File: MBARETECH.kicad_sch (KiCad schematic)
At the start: 48 parts, among them J10 Conn_01x03, J11 Conn_01x03, J17 Conn_01x03, J18 Conn_01x03, J19 TERMINAL DRIVER, J3 XT60-M, J7 Conn_01x03, J8 Conn_01x03, J9 Conn_01x03, SW1 SW_SPDT, SW2 SW_DIP_x04, SW3 SW_SPDT, SW5 SW_SPST, U2 ESP32-S3-DevKitC

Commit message: Version final
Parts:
- removed D1: D, symbol Device:D
- removed F1: Fuse, symbol Device:Fuse
- removed J19: TERMINAL DRIVER, symbol Connector:Screw_Terminal_01x02
- removed J3: XT60-M, XT60-M:AMASS_XT60-M, symbol XT60-M:XT60-M
- removed R20: R, symbol Device:R
- removed SW5: SW_SPST, symbol Switch:SW_SPST
- removed U2: ESP32-S3-DevKitC, PCM_Espressif:ESP32-S3-DevKitC, symbol Espressif:ESP32-S3-DevKitC
- added DRIVER1: DRIVER, TerminalBlock_Phoenix:TerminalBlock_Phoenix_MKDS-1,5-2-5.08_1x02_P5.08mm_Horizontal, symbol Connector:Screw_Terminal_01x02
- added IR6_NPN1: IR6, Connector_JST:JST_XH_B3B-XH-A_1x03_P2.50mm_Vertical, symbol Connector_Generic:Conn_01x03
- added IR7: IR7_NPN, Connector_JST:JST_XH_B3B-XH-A_1x03_P2.50mm_Vertical, symbol Connector_Generic:Conn_01x03
- added PWR1: PWR, TerminalBlock_Phoenix:TerminalBlock_Phoenix_MKDS-1,5-2-5.08_1x02_P5.08mm_Horizontal, symbol Connector:Screw_Terminal_01x02
- added R6, R7: 1Ok, Resistor_SMD:R_0603_1608Metric_Pad0.98x0.95mm_HandSolder, symbol Device:R
- added U1: ESP32-S3-DEVKITC-1-N8R2, ESP32-S3-DEVKITC-1-N8R2:XCVR_ESP32-S3-DEVKITC-1-N8R2, symbol ESP32-S3-DEVKITC-1-N8R2:ESP32-S3-DEVKITC-1-N8R2
- BUCK1: renamed from U3; value ~ -> BUCK_24V; footprint (none) -> Mbaretech_buckConverter:Buck-Converter
- BUCK2: renamed from U1; value ~ -> BUCK_3V3; footprint (none) -> Mbaretech_buckConverter:Buck-Converter
- Boost1: value ~ -> BOOST; footprint (none) -> Connector_PinHeader_2.54mm:PinHeader_1x03_P2.54mm_Vertical
- DIP1: renamed from SW2; value SW_DIP_x04 -> DIP; footprint (none) -> Button_Switch_THT:SW_DIP_SPSTx04_Slide_9.78x12.34mm_W7.62mm_P2.54mm
- EA1: renamed from J2; value ~ -> EA; footprint Connector_JST:JST_PH_B9B-PH-K_1x09_P2.00mm_Vertical -> Connector_JST:JST_XH_B3B-XH-A_1x03_P2.50mm_Vertical
- EB1: renamed from J4; value ~ -> EB; footprint Connector_JST:JST_PH_B9B-PH-K_1x09_P2.00mm_Vertical -> Connector_JST:JST_XH_B3B-XH-A_1x03_P2.50mm_Vertical
- HALL1: renamed from J5; value ~ -> HALL; footprint Connector_JST:JST_PH_B9B-PH-K_1x09_P2.00mm_Vertical -> Connector_JST:JST_XH_B3B-XH-A_1x03_P2.50mm_Vertical
- IMU1: renamed from U4; value ~ -> IMU; footprint (none) -> Connector_PinHeader_2.54mm:PinHeader_1x10_P2.54mm_Vertical
- IR1: renamed from J17; value Conn_01x03 -> IR1; footprint Connector_AMASS:AMASS_XT60-F_1x02_P7.20mm_Vertical -> Connector_JST:JST_XH_B3B-XH-A_1x03_P2.50mm_Vertical
- IR2: renamed from J7; value Conn_01x03 -> IR2; footprint Connector_AMASS:AMASS_XT60-F_1x02_P7.20mm_Vertical -> Connector_JST:JST_XH_B3B-XH-A_1x03_P2.50mm_Vertical
- IR3: renamed from J8; value Conn_01x03 -> IR3; footprint Connector_AMASS:AMASS_XT60-F_1x02_P7.20mm_Vertical -> Connector_JST:JST_XH_B3B-XH-A_1x03_P2.50mm_Vertical
- IR4: renamed from J9; value Conn_01x03 -> IR4; footprint Connector_AMASS:AMASS_XT60-F_1x02_P7.20mm_Vertical -> Connector_JST:JST_XH_B3B-XH-A_1x03_P2.50mm_Vertical
- IR5: renamed from J10; value Conn_01x03 -> IR5; footprint Connector_AMASS:AMASS_XT60-F_1x02_P7.20mm_Vertical -> Connector_JST:JST_XH_B3B-XH-A_1x03_P2.50mm_Vertical
- IR8: renamed from J18; value Conn_01x03 -> IR8_PNP; footprint Connector_AMASS:AMASS_XT60-F_1x02_P7.20mm_Vertical -> Connector_JST:JST_XH_B3B-XH-A_1x03_P2.50mm_Vertical
- IR9: renamed from J11; value Conn_01x03 -> IR9_PNP; footprint Connector_AMASS:AMASS_XT60-F_1x02_P7.20mm_Vertical -> Connector_JST:JST_XH_B3B-XH-A_1x03_P2.50mm_Vertical
- KS1: renamed from J6; value ~ -> KS; footprint Connector_JST:JST_PH_B9B-PH-K_1x09_P2.00mm_Vertical -> Connector_JST:JST_XH_B3B-XH-A_1x03_P2.50mm_Vertical
- LS1: renamed from J14; value ~ -> LS1; footprint Connector_JST:JST_PH_B9B-PH-K_1x09_P2.00mm_Vertical -> Connector_JST:JST_XH_B3B-XH-A_1x03_P2.50mm_Vertical
- LS2: renamed from J15; value ~ -> LS2; footprint Connector_JST:JST_PH_B9B-PH-K_1x09_P2.00mm_Vertical -> Connector_JST:JST_XH_B3B-XH-A_1x03_P2.50mm_Vertical
- LS3: renamed from J1; value ~ -> LS3; footprint Connector_JST:JST_PH_B9B-PH-K_1x09_P2.00mm_Vertical -> Connector_JST:JST_XH_B3B-XH-A_1x03_P2.50mm_Vertical
- LS4: renamed from J16; value ~ -> LS4; footprint Connector_JST:JST_PH_B9B-PH-K_1x09_P2.00mm_Vertical -> Connector_JST:JST_XH_B3B-XH-A_1x03_P2.50mm_Vertical
- MA1: renamed from J12; value ~ -> MA; footprint Connector_JST:JST_PH_B9B-PH-K_1x09_P2.00mm_Vertical -> Connector_JST:JST_XH_B3B-XH-A_1x03_P2.50mm_Vertical
- MB1: renamed from J13; value ~ -> MB; footprint Connector_JST:JST_PH_B9B-PH-K_1x09_P2.00mm_Vertical -> Connector_JST:JST_XH_B3B-XH-A_1x03_P2.50mm_Vertical
- R1, R10, R11, R2: footprint (none) -> Resistor_SMD:R_0603_1608Metric_Pad0.98x0.95mm_HandSolder
- R12: renamed from R3; footprint (none) -> Resistor_SMD:R_0603_1608Metric_Pad0.98x0.95mm_HandSolder
- R13: renamed from R7; footprint (none) -> Resistor_SMD:R_0603_1608Metric_Pad0.98x0.95mm_HandSolder
- R14: renamed from R4; value `5k -> 5k; footprint (none) -> Resistor_SMD:R_0603_1608Metric_Pad0.98x0.95mm_HandSolder
- R15: renamed from R5; footprint (none) -> Resistor_SMD:R_0603_1608Metric_Pad0.98x0.95mm_HandSolder
- R16: renamed from R14; footprint (none) -> Resistor_SMD:R_0603_1608Metric_Pad0.98x0.95mm_HandSolder
- R17: renamed from R15; footprint (none) -> Resistor_SMD:R_0603_1608Metric_Pad0.98x0.95mm_HandSolder
- R18: renamed from R16; footprint (none) -> Resistor_SMD:R_0603_1608Metric_Pad0.98x0.95mm_HandSolder
- R19: renamed from R17; footprint (none) -> Resistor_SMD:R_0603_1608Metric_Pad0.98x0.95mm_HandSolder
- R3: renamed from R6; footprint (none) -> Resistor_SMD:R_0603_1608Metric_Pad0.98x0.95mm_HandSolder
- R4: renamed from R8; footprint (none) -> Resistor_SMD:R_0603_1608Metric_Pad0.98x0.95mm_HandSolder
- R5: renamed from R9; footprint (none) -> Resistor_SMD:R_0603_1608Metric_Pad0.98x0.95mm_HandSolder
- R8: renamed from R18; footprint (none) -> Resistor_SMD:R_0603_1608Metric_Pad0.98x0.95mm_HandSolder
- R9: renamed from R19; footprint (none) -> Resistor_SMD:R_0603_1608Metric_Pad0.98x0.95mm_HandSolder
- SW1: value SW_SPDT -> SW1; footprint (none) -> SPDT_SlideSwitch:tht
- SW2: renamed from SW3; value SW_SPDT -> SW2; footprint (none) -> SPDT_SlideSwitch:tht
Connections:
- net 24V is gone; now on net +24V: BUCK1.4 (VOUT)
- net GNDS is gone; now on net GND: IR2.3 (Pin_3), IR4.3 (Pin_3)
- net +24V: now also IR8.1 (Pin_1), IR9.1 (Pin_1), IR6_NPN1.1 (Pin_1), IR7.1 (Pin_1); no longer IR8.3 (Pin_3), IR9.3 (Pin_3)
- net +3V3: now also R2.1, R6.1, R7.1, U1.J1_1 (3V3), U1.J1_2 (3V3); no longer R13.1
- net +5V: now also DRIVER1.1 (Pin_1)
- net +BATT: now also PWR1.1 (Pin_1)
- net -BATT: now also PWR1.2 (Pin_2)
- net A0: now also U1.J3_15 (GPIO45)
- net A1: now also U1.J3_16 (GPIO48)
- net B0: now also U1.J3_12 (GPIO36)
- net B1: now also U1.J3_13 (GPIO35)
- net ENCODER_A_3V3: now also R13.1, U1.J1_20 (GPIO14); no longer R2.1
- net ENCODER_B_3V3: now also U1.J1_18 (GPIO12)
- net GND: now also IR8.3 (Pin_3), IR9.3 (Pin_3), R13.2, DRIVER1.2 (Pin_2), IR6_NPN1.3 (Pin_3), IR7.3 (Pin_3), U1.J1_22 (GND), U1.J3_1 (GND), U1.J3_21 (GND), U1.J3_22 (GND); no longer IR8.1 (Pin_1), IR9.1 (Pin_1), R2.2
- net HALL_3V3: now also U1.J3_2 (U0TXD/GPIO43)
- net IR1_3V3: now also R1.2, U1.J3_8 (MTDO/GPIO40); no longer R13.2
- net IR2_3V3: now also R2.2, U1.J3_9 (MTCK/GPIO39); no longer R1.2
- net IR3_3V3: now also U1.J3_10 (GPIO38)
- net IR4_3V3: now also U1.J1_11 (GPIO18)
- net IR5_3V3: now also U1.J1_10 (GPIO17)
- net IR6_3V3: now also IR6_NPN1.2 (Pin_2), R6.2, U1.J1_4 (GPIO4); no longer R8.1, R9.1
- net IR7_3V3: now also IR7.2 (Pin_2), R7.2, U1.J1_5 (GPIO5); no longer R10.1, R11.1
- net KILLSWITCH: now also U1.J3_7 (MTDI/GPIO41)
- net LS1_3V3: now also U1.J1_13 (GPIO3)
- net LS2_3V3: now also U1.J1_12 (GPIO8)
- net LS3_3V3: now also U1.J3_19 (USB_D+/GPIO20)
- net LS4_3V3: now also U1.J3_20 (USB_D-/GPIO19)
- net PWMA: now also U1.J3_14 (GPIO0)
- net PWMB: now also U1.J3_11 (GPIO37)
- net S1: now also U1.J3_6 (MTMS/GPIO42)
- net S2: now also U1.J3_5 (GPIO2)
- net S3: now also U1.J3_4 (GPIO1)
- net S4: now also U1.J3_3 (U0RXD/GPIO44)
- net SCL: now also U1.J1_9 (GPIO16)
- net SDA: now also U1.J1_8 (GPIO15)
- net IMU_INT: no longer names the net of IMU1.8 (INT)
- net IR6_24V renamed IR8_24V
- net IR7_24V renamed IR9_24V
- new net IR8_3V3_PNP: R8.1, R9.1, U1.J1_6 (GPIO6)
- new net IR9_3V3_PNP: R10.1, R11.1, U1.J1_7 (GPIO7)
- no-connect marks 8 -> 17
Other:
- moved on the sheet: BUCK1, BUCK2, Boost1, DIP1, EA1, EB1, HALL1, IMU1, IR2, IR3, IR4, IR5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

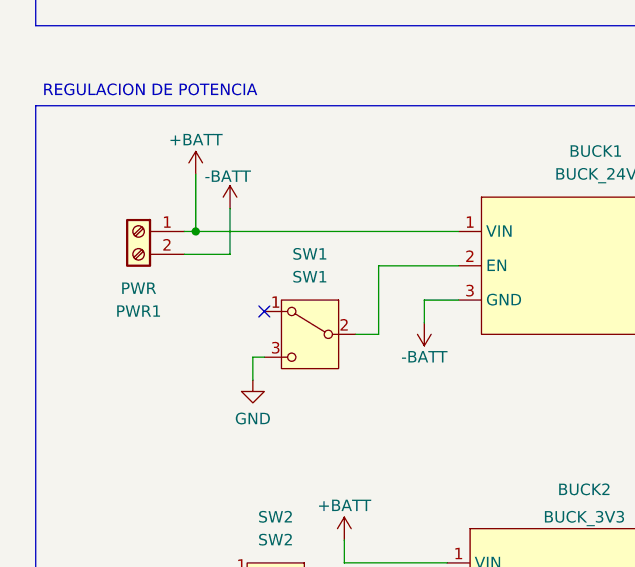
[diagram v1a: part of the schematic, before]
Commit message: Connect -BATT2GND
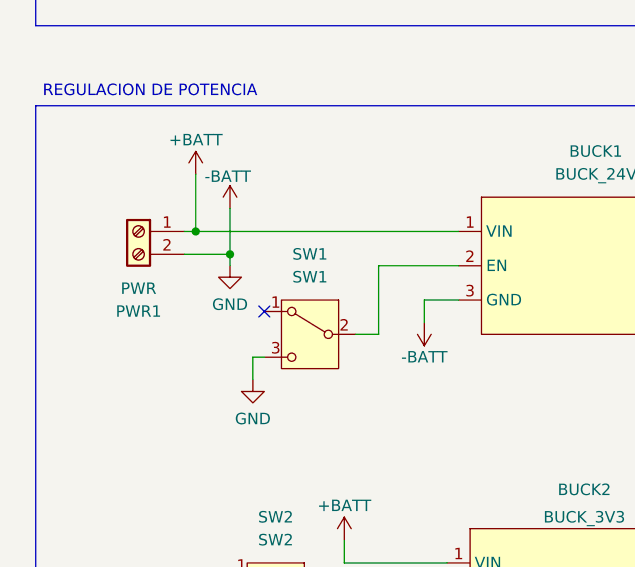
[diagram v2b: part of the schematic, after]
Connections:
- net GND is gone; now on net -BATT: BUCK1.5 (GND), BUCK2.5 (GND), Boost1.2 (GND), DRIVER1.2 (Pin_2), EA1.3 (Pin_3), EB1.3 (Pin_3), HALL1.3 (Pin_3), IMU1.2 (GND), IR1.3 (Pin_3), IR2.3 (Pin_3), IR3.3 (Pin_3), IR4.3 (Pin_3), IR5.3 (Pin_3), IR6_NPN1.3 (Pin_3), IR7.3 (Pin_3), IR8.3 (Pin_3), IR9.3 (Pin_3), KS1.3 (Pin_3), LS1.3 (Pin_3), LS2.3 (Pin_3), LS3.3 (Pin_3), LS4.3 (Pin_3), R11.2, R13.2, R15.2, R16.2, R17.2, R18.2, R19.2, R9.2, SW1.3 (C), SW2.3 (C), U1.J1_22 (GND), U1.J3_1 (GND), U1.J3_21 (GND), U1.J3_22 (GND)
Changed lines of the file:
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@@
 		(color 0 0 0 0)
 	)
+	(junction
+		(at 59.69 143.51)
+		(diameter 0)
+		(color 0 0 0 0)
+	)
 	(no_connect
 		(at 109.22 39.37)
@@
 	(wire
 		(pts
+			(xy 59.69 144.78) (xy 59.69 143.51)
+		)
+		(stroke
+			(width 0)
+			(type default)
+		)
+	)
+	(wire
+		(pts
 			(xy 90.17 209.55) (xy 90.17 210.82)
 		)
@@
 					(unit 1)
 				)
+			)
+		)
+	)
+	(symbol
+		(lib_id "power:GND")
+		(at 59.69 144.78 0)
+		(unit 1)
+		(exclude_from_sim no)
+		(in_bom yes)
+		(on_board yes)
+		(dnp no)
+		(property "Reference" "#PWR01"
+			(at 59.69 151.13 0)
+			(effects
+				(font
+					(size 1.27 1.27)
+				)
+				(hide yes)
+			)
+		)
+		(property "Value" "GND"
+			(at 59.69 149.098 0)
+			(effects
+				(font
+					(size 1.27 1.27)
+				)
+			)
+		)
+		(property "Footprint" ""
+			(at 59.69 144.78 0)
+			(effects
+				(font
+					(size 1.27 1.27)
+				)
+				(hide yes)
+			)
+		)
+		(property "Datasheet" ""
+			(at 59.69 144.78 0)
+			(effects
+				(font
+					(size 1.27 1.27)
+				)
+				(hide yes)
+			)
+		)
+		(property "Description" "Power symbol creates a global label with name \"GND\" , ground"
+			(at 59.69 144.78 0)
+			(effects
+				(font
+					(size 1.27 1.27)
+				)
+				(hide yes)
+			)
+		)
+		(pin "1"
+		)
+		(instances
+			(project "MBARETECH"
+				(path "/22b8a1e8-4df5-4930-9e5c-6226e609bfdf"
+					(reference "#PWR01")
+					(unit 1)
+				)

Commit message: final
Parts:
- R1: value 1Ok -> R1
- R10: value R -> R10
- R11: value R -> R11
- R12: value `5k -> R12
- R13: value 1Ok -> R13
- R14: value 5k -> R14
- R15: value 10k -> R15
- R16: value 10k -> R16
- R17: value 10k -> R17
- R18: value 10k -> R18
- R19: value 10k -> R19
- R2: value 10k -> R2
- R3: value 1Ok -> R3
- R4: value 1Ok -> R4
- R5: value 1Ok -> R5
- R6: value 1Ok -> R6
- R7: value 1Ok -> R7
- R8: value R -> R8
- R9: value R -> R9
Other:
- moved on the sheet: SW1
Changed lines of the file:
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@@
 	)
 	(junction
+		(at 55.88 143.51)
+		(diameter 0)
+		(color 0 0 0 0)
+	)
+	(junction
 		(at 55.88 140.97)
 		(diameter 0)
@@
 		(color 0 0 0 0)
 	)
-	(junction
-		(at 59.69 143.51)
-		(diameter 0)
-		(color 0 0 0 0)
-	)
 	(no_connect
 		(at 109.22 39.37)
@@
 	)
 	(no_connect
-		(at 63.5 149.86)
+		(at 64.77 149.86)
 	)
 	(no_connect
@@
 	(wire
 		(pts
-			(xy 59.69 138.43) (xy 59.69 143.51)
+			(xy 55.88 144.78) (xy 55.88 143.51)
 		)
 		(stroke
@@
 	(wire
 		(pts
-			(xy 62.23 154.94) (xy 63.5 154.94)
+			(xy 62.23 154.94) (xy 64.77 154.94)
 		)
 		(stroke
@@
 	(wire
 		(pts
-			(xy 76.2 152.4) (xy 73.66 152.4)
+			(xy 76.2 152.4) (xy 74.93 152.4)
 		)
 		(stroke
@@
 	(wire
 		(pts
+			(xy 60.96 144.78) (xy 60.96 143.51)
+		)
+		(stroke
+			(width 0)
+			(type default)
+		)
+	)
+	(wire
+		(pts
 			(xy 115.57 140.97) (xy 118.11 140.97)
 		)
@@
 	(wire
 		(pts
-			(xy 54.61 143.51) (xy 59.69 143.51)
+			(xy 54.61 143.51) (xy 55.88 143.51)
 		)
 		(stroke
@@
 	(wire
 		(pts
+			(xy 55.88 143.51) (xy 60.96 143.51)
+		)
+		(stroke
+			(width 0)
+			(type default)
+		)
+	)
+	(wire
+		(pts
 			(xy 350.52 33.02) (xy 350.52 40.64)
 		)
@@
 	(wire
 		(pts
-			(xy 59.69 144.78) (xy 59.69 143.51)
-		)
-		(stroke
-			(width 0)
-			(type default)
-		)
-	)
-	(wire
-		(pts
 			(xy 90.17 209.55) (xy 90.17 210.82)
 		)
@@
 			)
 		)
-		(property "Value" "10k"
+		(property "Value" "R19"
 			(at 220.218 238.76 0)
 			(effects
@@
 			)
 		)
-		(property "Value" "10k"
+		(property "Value" "R16"
 			(at 200.66 238.76 0)
 			(effects
@@
 	(symbol
 		(lib_id "power:+BATT")
-		(at 59.69 138.43 0)
+		(at 55.88 144.78 180)
 		(unit 1)
 		(exclude_from_sim no)
@@
 		(dnp no)
 		(property "Reference" "#PWR042"
-			(at 59.69 142.24 0)
+			(at 55.88 140.97 0)
 			(effects
 				(font
@@
 		)
 		(property "Value" "-BATT"
-			(at 59.436 134.874 0)
+			(at 56.134 148.336 0)
 			(effects
 				(font
@@
 		)
 		(property "Footprint" ""
-			(at 59.69 138.43 0)
+			(at 55.88 144.78 0)
 			(effects
 				(font
@@
 		)
 		(property "Datasheet" ""
-			(at 59.69 138.43 0)
+			(at 55.88 144.78 0)
 			(effects
 				(font
@@
 		)
 		(property "Description" "Power symbol creates a global label with name \"+BATT\""
-			(at 59.69 138.43 0)
+			(at 55.88 144.78 0)
 			(effects
 				(font
@@
 			)
 		)
-		(property "Value" "R"
+		(property "Value" "R10"
 			(at 314.96 232.41 90)
 			(effects
@@
 			)
 		)
-		(property "Value" "1Ok"
+		(property "Value" "R5"
 			(at 313.69 115.5699 0)
 			(effects
@@
 			)
 		)
-		(property "Value" "1Ok"
+		(property "Value" "R4"
 			(at 365.76 77.4699 0)
 			(effects
@@
 			)
 		)
-		(property "Value" "R"
+		(property "Value" "R8"
 			(at 312.42 198.12 90)
 			(effects
@@
 			)
 		)
-		(property "Value" "1Ok"
+		(property "Value" "R3"
 			(at 313.69 76.1999 0)
 			(effects
@@
 			)
 		)
-		(property "Value" "R"
+		(property "Value" "R11"
 			(at 322.58 233.6799 0)
 			(effects
@@
 			)
 		)
-		(property "Value" "5k"
+		(property "Value" "R14"
 			(at 193.04 165.1 0)
 			(effects
@@
 			)
 		)
-		(property "Value" "1Ok"
+		(property "Value" "R7"
 			(at 317.5 151.1299 0)
 			(effects
@@
 			)
 		)
-		(property "Value" "1Ok"
+		(property "Value" "R1"
 			(at 313.69 39.3699 0)
 			(effects
@@
 			)
 		)
-		(property "Value" "10k"
+		(property "Value" "R15"
 			(at 200.66 172.72 0)
 			(effects
@@
 	)
 	(symbol
+		(lib_id "power:GND")
+		(at 60.96 144.78 0)
+		(unit 1)
+		(exclude_from_sim no)
+		(in_bom yes)
+		(on_board yes)
+		(dnp no)
+		(property "Reference" "#PWR03"
+			(at 60.96 151.13 0)
+			(effects
+				(font
+					(size 1.27 1.27)
+				)
+				(hide yes)
+			)
+		)
+		(property "Value" "GND"
+			(at 60.96 149.098 0)
+			(effects
+				(font
+					(size 1.27 1.27)
+				)
+			)
+		)
+		(property "Footprint" ""
+			(at 60.96 144.78 0)
+			(effects
+				(font
+					(size 1.27 1.27)
+				)
+				(hide yes)
+			)
+		)
+		(property "Datasheet" ""
+			(at 60.96 144.78 0)
+			(effects
+				(font
+					(size 1.27 1.27)
+				)
+				(hide yes)
+			)
+		)
+		(property "Description" "Power symbol creates a global label with name \"GND\" , ground"
+			(at 60.96 144.78 0)
+			(effects
+				(font
+					(size 1.27 1.27)
+				)
+				(hide yes)
+			)
+		)
+		(pin "1"
+		)
+		(instances
+			(project "MBARETECH"
+				(path "/22b8a1e8-4df5-4930-9e5c-6226e609bfdf"
+					(reference "#PWR03")
+					(unit 1)
+				)
+			)
+		)
+	)
+	(symbol
 		(lib_id "power:+3V3")
 		(at 213.36 35.56 0)
@@
 			)
 		)
-		(property "Value" "10k"
+		(property "Value" "R2"
 			(at 361.95 39.37 0)
 			(effects
@@
 	(symbol
 		(lib_id "power:GND")
-		(at 59.69 144.78 0)
-		(unit 1)
-		(exclude_from_sim no)
-		(in_bom yes)
-		(on_board yes)
-		(dnp no)
-		(property "Reference" "#PWR01"
-			(at 59.69 151.13 0)
-			(effects
-				(font
-					(size 1.27 1.27)
-				)
-				(hide yes)
-			)
-		)
-		(property "Value" "GND"
-			(at 59.69 149.098 0)
-			(effects
-				(font
-					(size 1.27 1.27)
-				)
-			)
-		)
-		(property "Footprint" ""
-			(at 59.69 144.78 0)
-			(effects
-				(font
-					(size 1.27 1.27)
-				)
-				(hide yes)
-			)
-		)
-		(property "Datasheet" ""
-			(at 59.69 144.78 0)
-			(effects
-				(font
-					(size 1.27 1.27)
-				)
-				(hide yes)
-			)
-		)
-		(property "Description" "Power symbol creates a global label with name \"GND\" , ground"
-			(at 59.69 144.78 0)
-			(effects
-				(font
-					(size 1.27 1.27)
-				)
-				(hide yes)
-			)
-		)
-		(pin "1"
-		)
-		(instances
-			(project "MBARETECH"
-				(path "/22b8a1e8-4df5-4930-9e5c-6226e609bfdf"
-					(reference "#PWR01")
-					(unit 1)
-				)
-			)
-		)
-	)
-	(symbol
-		(lib_id "power:GND")
 		(at 118.11 151.13 0)
 		(unit 1)
@@
 			)
 		)
-		(property "Value" "10k"
+		(property "Value" "R18"
 			(at 213.36 238.76 0)
 			(effects
@@
 			)
 		)
-		(property "Value" "10k"
+		(property "Value" "R17"
 			(at 207.01 238.76 0)
 			(effects
@@
 			)
 		)
-		(property "Value" "`5k"
+		(property "Value" "R12"
 			(at 194.31 135.89 0)
 			(effects
@@
 			)
 		)
-		(property "Value" "1Ok"
+		(property "Value" "R13"
 			(at 200.66 143.5099 0)
 			(effects
@@
 	(symbol
 		(lib_id "Switch:SW_SPDT")
-		(at 68.58 152.4 0)
+		(at 69.85 152.4 0)
 		(mirror y)
 		(unit 1)
@@
 		(dnp no)
 		(property "Reference" "SW1"
-			(at 68.58 143.51 0)
+			(at 69.85 143.51 0)
 			(effects
 				(font
@@
 		)
 		(property "Value" "SW1"
-			(at 68.58 146.05 0)
+			(at 69.85 146.05 0)
 			(effects
 				(font
@@
 		)
 		(property "Footprint" "SPDT_SlideSwitch:tht"
-			(at 68.58 152.4 0)
+			(at 69.85 152.4 0)
 			(effects
 				(font
@@
 		)
 		(property "Datasheet" "~"
-			(at 68.58 160.02 0)
+			(at 69.85 160.02 0)
 			(effects
 				(font
@@
 		)
 		(property "Description" "Switch, single pole double throw"
-			(at 68.58 152.4 0)
+			(at 69.85 152.4 0)
 			(effects
 				(font
@@
 			)
 		)
-		(property "Value" "1Ok"
+		(property "Value" "R6"
 			(at 369.57 115.5699 0)
 			(effects
@@
 			)
 		)
-		(property "Value" "R"
+		(property "Value" "R9"
 			(at 320.04 208.2799 0)
 			(effects
